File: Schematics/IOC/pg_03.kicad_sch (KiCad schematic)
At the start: 78 parts, among them U401 F245, U402 F245, U403 F245, U404 F245, U405 F244, U406 F244, U407 F244, U408 F244, U409 F04, U410 F04, U411 F04, U412 F163, U413 F04, U414 F02

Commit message: Align to grid
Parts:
- removed GF103, GF107, GF11, GF111, GF115, GF119, GF123, GF127, GF15, GF167, GF171, GF175, GF179, GF183, GF187, GF19, GF191, GF195, GF199, GF203, GF207, GF211, GF215, GF219, GF223, GF227, GF23, GF231, GF235, GF239, GF243, GF247, GF251, GF255, GF259, GF263, GF267, GF27, GF271, GF275, GF279, GF283, GF287, GF291, GF3, GF31, GF35, GF39, GF43, GF47, GF51, GF55, GF59, GF63, GF67, GF7, GF71, GF75, GF79, GF83, GF87, GF91, GF95, GF99: GF, symbol r1000:GF
- removed U401, U402, U403, U404: F245, symbol r1000:F245
- removed U405, U406, U407, U408: F244, symbol r1000:F244
- removed U409, U410, U411, U413: F04, symbol r1000:F04
- removed U412: F163, symbol r1000:F163
- removed U414: F02, symbol r1000:F02
- added U (x64): (no value), symbol r1000:GF
- added U (x4): (no value), symbol r1000:F04
- added U (x4): (no value), symbol r1000:F245
- added U (x4): (no value), symbol r1000:F244
- added U: (no value), symbol r1000:F02
- added U: (no value), symbol r1000:F163
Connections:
- net 68K.A0: now also U.2 (D1), U.2 (I0)
- net 68K.A1: now also U.4 (I1)
- net 68K.A10: now also U.6 (I2)
- net 68K.A11: now also U.8 (I3)
- net 68K.A12: now also U.11 (I4)
- net 68K.A13: now also U.13 (I5)
- net 68K.A14: now also U.15 (I6)
- net 68K.A15: now also U.17 (I7)
- net 68K.A16: now also U.2 (I0)
- net 68K.A17: now also U.4 (I1)
- net 68K.A18: now also U.6 (I2)
- net 68K.A19: now also U.8 (I3)
- net 68K.A2: now also U.6 (I2)
- net 68K.A20: now also U.11 (I4)
- net 68K.A21: now also U.13 (I5)
- net 68K.A22: now also U.15 (I6)
- net 68K.A23: now also U.17 (I7)
- net 68K.A24: now also U.2 (I0)
- net 68K.A25: now also U.4 (I1)
- net 68K.A26: now also U.6 (I2)
- net 68K.A27: now also U.8 (I3)
- net 68K.A28: now also U.11 (I4)
- net 68K.A29: now also U.13 (I5)
- net 68K.A3: now also U.8 (I3)
- net 68K.A30: now also U.15 (I6)
- net 68K.A31: now also U.17 (I7)
- net 68K.A4: now also U.11 (I4)
- net 68K.A5: now also U.13 (I5)
- net 68K.A6: now also U.15 (I6)
- net 68K.A7: now also U.17 (I7)
- net 68K.A8: now also U.2 (I0)
- net 68K.A9: now also U.4 (I1)
- net 68K.D0: now also U.2 (A0)
- net 68K.D1: now also U.3 (A1)
- net 68K.D10: now also U.4 (A2)
- net 68K.D11: now also U.5 (A3)
- net 68K.D12: now also U.6 (A4)
- net 68K.D13: now also U.7 (A5)
- net 68K.D14: now also U.8 (A6)
- net 68K.D15: now also U.9 (A7)
- net 68K.D16: now also U.2 (A0)
- net 68K.D17: now also U.3 (A1)
- net 68K.D18: now also U.4 (A2)
- net 68K.D19: now also U.5 (A3)
- net 68K.D2: now also U.4 (A2)
- net 68K.D20: now also U.6 (A4)
- net 68K.D21: now also U.7 (A5)
- net 68K.D22: now also U.8 (A6)
- net 68K.D23: now also U.9 (A7)
- net 68K.D24: now also U.2 (A0)
- net 68K.D25: now also U.3 (A1)
- net 68K.D26: now also U.4 (A2)
- net 68K.D27: now also U.5 (A3)
- net 68K.D28: now also U.6 (A4)
- net 68K.D29: now also U.7 (A5)
- net 68K.D3: now also U.5 (A3)
- net 68K.D30: now also U.8 (A6)
- net 68K.D31: now also U.9 (A7)
- net 68K.D4: now also U.6 (A4)
- net 68K.D5: now also U.7 (A5)
- net 68K.D6: now also U.8 (A6)
- net 68K.D7: now also U.9 (A7)
- net 68K.D8: now also U.2 (A0)
- net 68K.D9: now also U.3 (A1)
- net BOOTTIME: now also U.1 (D0), U.2 (Q), U.7 (ENP)
- net CLK.2X.B3: now also U.2 (CLK)
- net CYCLE_END: now also U.10 (ENT)
- net DBEN~: now also U.19 (OE), U.19 (OE), U.19 (OE), U.19 (OE)
- net IOP.A0~: now also U.1, U.3 (Q)
- net IOP.A1: now also U.1, U.16 (Y1)
- net IOP.A10: now also U.1, U.14 (Y2)
- net IOP.A11: now also U.1, U.12 (Y3)
- net IOP.A12: now also U.1, U.9 (Y4)
- net IOP.A13: now also U.1, U.7 (Y5)
- net IOP.A14: now also U.1, U.5 (Y6)
- net IOP.A15: now also U.1, U.3 (Y7)
- net IOP.A16: now also U.1, U.18 (Y0)
- net IOP.A17: now also U.1, U.16 (Y1)
- net IOP.A18: now also U.1, U.14 (Y2)
- net IOP.A19: now also U.1, U.12 (Y3)
- net IOP.A2: now also U.1, U.14 (Y2)
- net IOP.A20: now also U.1, U.9 (Y4)
- net IOP.A21: now also U.1, U.7 (Y5)
- net IOP.A22: now also U.1, U.5 (Y6)
- net IOP.A23: now also U.1, U.3 (Y7)
- net IOP.A24: now also U.1, U.18 (Y0)
- net IOP.A25: now also U.1, U.16 (Y1)
- net IOP.A26: now also U.1, U.14 (Y2)
- net IOP.A27: now also U.1, U.12 (Y3)
- net IOP.A28: now also U.1, U.9 (Y4)
- net IOP.A29: now also U.1, U.7 (Y5)
- net IOP.A3: now also U.1, U.12 (Y3)
- net IOP.A30: now also U.1, U.5 (Y6)
- net IOP.A31: now also U.1, U.3 (Y7)
- net IOP.A4: now also U.1, U.9 (Y4)
- net IOP.A5: now also U.1, U.7 (Y5)
- net IOP.A6: now also U.1, U.5 (Y6)
- net IOP.A7: now also U.1, U.3 (Y7)
- net IOP.A8: now also U.1, U.18 (Y0)
- net IOP.A9: now also U.1, U.16 (Y1)
- net IOP.D0: now also U.1, U.18 (B0)
- net IOP.D1: now also U.1, U.17 (B1)
- net IOP.D10: now also U.1, U.16 (B2)
- net IOP.D11: now also U.1, U.15 (B3)
- net IOP.D12: now also U.1, U.14 (B4)
- net IOP.D13: now also U.1, U.13 (B5)
- net IOP.D14: now also U.1, U.12 (B6)
- net IOP.D15: now also U.1, U.11 (B7)
- net IOP.D16: now also U.1, U.18 (B0)
- net IOP.D17: now also U.1, U.17 (B1)
- net IOP.D18: now also U.1, U.16 (B2)
- net IOP.D19: now also U.1, U.15 (B3)
- net IOP.D2: now also U.1, U.16 (B2)
- net IOP.D20: now also U.1, U.14 (B4)
- net IOP.D21: now also U.1, U.13 (B5)
- net IOP.D22: now also U.1, U.12 (B6)
- net IOP.D23: now also U.1, U.11 (B7)
- net IOP.D24: now also U.1, U.18 (B0)
- net IOP.D25: now also U.1, U.17 (B1)
- net IOP.D26: now also U.1, U.16 (B2)
- net IOP.D27: now also U.1, U.15 (B3)
- net IOP.D28: now also U.1, U.14 (B4)
- net IOP.D29: now also U.1, U.13 (B5)
- net IOP.D3: now also U.1, U.15 (B3)
- net IOP.D30: now also U.1, U.12 (B6)
- net IOP.D31: now also U.1, U.11 (B7)
- net IOP.D4: now also U.1, U.14 (B4)
- net IOP.D5: now also U.1, U.13 (B5)
- net IOP.D6: now also U.1, U.12 (B6)
- net IOP.D7: now also U.1, U.11 (B7)
- net IOP.D8: now also U.1, U.18 (B0)
- net IOP.D9: now also U.1, U.17 (B1)
- net IOP.WR.B0: now also U.1 (D0), U.1 (DIR), U.1 (DIR), U.1 (DIR), U.1 (DIR), U.2 (Q)
- net IOP.WR.B1: now also U.2 (Q)
- net IOP.WR~: now also U.2 (Q)
- net IOP_RESET~: now also U.1 (CLR)
- net PD: now also U.1 (OE0), U.1 (OE0), U.1 (OE0), U.1 (OE0), U.19 (OE1), U.19 (OE1), U.19 (OE1), U.19 (OE1)
- net PU: now also U.9 (LD)
- net WR~: now also U.1 (D0), U.1 (D0)
- new net: U.1 (D0), U.11 (Q0)

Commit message: TYP/VAL busses
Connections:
- net 68K.D0: now also U.3 (A0); no longer U.2 (A0)
- net 68K.D1: now also U.5 (A1); no longer U.3 (A1)
- net 68K.D10: now also U.7 (A2); no longer U.4 (A2)
- net 68K.D11: now also U.9 (A3); no longer U.5 (A3)
- net 68K.D12: now also U.11 (A4); no longer U.6 (A4)
- net 68K.D13: now also U.13 (A5); no longer U.7 (A5)
- net 68K.D14: now also U.15 (A6); no longer U.8 (A6)
- net 68K.D15: now also U.17 (A7); no longer U.9 (A7)
- net 68K.D16: now also U.3 (A0); no longer U.2 (A0)
- net 68K.D17: now also U.5 (A1); no longer U.3 (A1)
- net 68K.D18: now also U.7 (A2); no longer U.4 (A2)
- net 68K.D19: now also U.9 (A3); no longer U.5 (A3)
- net 68K.D2: now also U.7 (A2); no longer U.4 (A2)
- net 68K.D20: now also U.11 (A4); no longer U.6 (A4)
- net 68K.D21: now also U.13 (A5); no longer U.7 (A5)
- net 68K.D22: now also U.15 (A6); no longer U.8 (A6)
- net 68K.D23: now also U.17 (A7); no longer U.9 (A7)
- net 68K.D24: now also U.3 (A0); no longer U.2 (A0)
- net 68K.D25: now also U.5 (A1); no longer U.3 (A1)
- net 68K.D26: now also U.7 (A2); no longer U.4 (A2)
- net 68K.D27: now also U.9 (A3); no longer U.5 (A3)
- net 68K.D28: now also U.11 (A4); no longer U.6 (A4)
- net 68K.D29: now also U.13 (A5); no longer U.7 (A5)
- net 68K.D3: now also U.9 (A3); no longer U.5 (A3)
- net 68K.D30: now also U.15 (A6); no longer U.8 (A6)
- net 68K.D31: now also U.17 (A7); no longer U.9 (A7)
- net 68K.D4: now also U.11 (A4); no longer U.6 (A4)
- net 68K.D5: now also U.13 (A5); no longer U.7 (A5)
- net 68K.D6: now also U.15 (A6); no longer U.8 (A6)
- net 68K.D7: now also U.17 (A7); no longer U.9 (A7)
- net 68K.D8: now also U.3 (A0); no longer U.2 (A0)
- net 68K.D9: now also U.5 (A1); no longer U.3 (A1)
- net BOOTTIME: now also U.13 (ENP); no longer U.7 (ENP)
- net CLK.2X.B3: now also U.1 (CLK); no longer U.2 (CLK)
- net CYCLE_END: now also U.14 (ENT); no longer U.10 (ENT)
- net DBEN~: now also U.2 (OE), U.2 (OE), U.2 (OE), U.2 (OE); no longer U.19 (OE), U.19 (OE), U.19 (OE), U.19 (OE)
- net IOP.D0: now also U.4 (B0); no longer U.18 (B0)
- net IOP.D1: now also U.6 (B1); no longer U.17 (B1)
- net IOP.D10: now also U.8 (B2); no longer U.16 (B2)
- net IOP.D11: now also U.10 (B3); no longer U.15 (B3)
- net IOP.D12: now also U.12 (B4); no longer U.14 (B4)
- net IOP.D13: now also U.14 (B5); no longer U.13 (B5)
- net IOP.D14: now also U.16 (B6); no longer U.12 (B6)
- net IOP.D15: now also U.18 (B7); no longer U.11 (B7)
- net IOP.D16: now also U.4 (B0); no longer U.18 (B0)
- net IOP.D17: now also U.6 (B1); no longer U.17 (B1)
- net IOP.D18: now also U.8 (B2); no longer U.16 (B2)
- net IOP.D19: now also U.10 (B3); no longer U.15 (B3)
- net IOP.D2: now also U.8 (B2); no longer U.16 (B2)
- net IOP.D20: now also U.12 (B4); no longer U.14 (B4)
- net IOP.D21: now also U.14 (B5); no longer U.13 (B5)
- net IOP.D22: now also U.16 (B6); no longer U.12 (B6)
- net IOP.D23: now also U.18 (B7); no longer U.11 (B7)
- net IOP.D24: now also U.4 (B0); no longer U.18 (B0)
- net IOP.D25: now also U.6 (B1); no longer U.17 (B1)
- net IOP.D26: now also U.8 (B2); no longer U.16 (B2)
- net IOP.D27: now also U.10 (B3); no longer U.15 (B3)
- net IOP.D28: now also U.12 (B4); no longer U.14 (B4)
- net IOP.D29: now also U.14 (B5); no longer U.13 (B5)
- net IOP.D3: now also U.10 (B3); no longer U.15 (B3)
- net IOP.D30: now also U.16 (B6); no longer U.12 (B6)
- net IOP.D31: now also U.18 (B7); no longer U.11 (B7)
- net IOP.D4: now also U.12 (B4); no longer U.14 (B4)
- net IOP.D5: now also U.14 (B5); no longer U.13 (B5)
- net IOP.D6: now also U.16 (B6); no longer U.12 (B6)
- net IOP.D7: now also U.18 (B7); no longer U.11 (B7)
- net IOP.D8: now also U.4 (B0); no longer U.18 (B0)
- net IOP.D9: now also U.6 (B1); no longer U.17 (B1)
- net IOP_RESET~: now also U.3 (CLR); no longer U.1 (CLR)
- net PU: now also U.2 (LD); no longer U.9 (LD)
- net at U.11 (D3): no longer U.1 (D0)
- net at U.6 (Q0): now also U.1 (D0)

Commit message: IOC: dedup, clocks, dfsm
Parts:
- removed U: (no value), symbol r1000:F04
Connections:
- net CLK.2X.B3 renamed CLK.2X
- net IOP.WR.B0 renamed IOP.WR
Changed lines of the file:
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@@
   (junction (at 203.2 142.24) (diameter 0) (color 0 0 0 0)
   )
-  (junction (at 48.26 17.78) (diameter 0) (color 0 0 0 0)
-  )
   (junction (at 76.2 139.7) (diameter 0) (color 0 0 0 0)
   )
@@
     (stroke (width 0) (type default))
   )
-  (wire (pts (xy 48.26 35.56) (xy 48.26 17.78))
-    (stroke (width 0) (type default))
-  )
   (wire (pts (xy 487.68 68.58) (xy 492.76 68.58))
     (stroke (width 0) (type default))
@@
     (stroke (width 0) (type default))
   )
-  (wire (pts (xy 58.42 35.56) (xy 48.26 35.56))
-    (stroke (width 0) (type default))
-  )
   (wire (pts (xy 93.98 287.02) (xy 76.2 287.02))
     (stroke (width 0) (type default))
@@
     (stroke (width 0) (type default))
   )
-  (wire (pts (xy 40.64 17.78) (xy 48.26 17.78))
-    (stroke (width 0) (type default))
-  )
   (bus (pts (xy 246.38 182.88) (xy 246.38 187.96))
     (stroke (width 0) (type default))
@@
     (stroke (width 0) (type default))
   )
-  (wire (pts (xy 78.74 35.56) (xy 104.14 35.56))
-    (stroke (width 0) (type default))
-  )
   (bus (pts (xy 246.38 114.3) (xy 246.38 119.38))
     (stroke (width 0) (type default))
@@
     (stroke (width 0) (type default))
   )
-  (wire (pts (xy 48.26 17.78) (xy 58.42 17.78))
+  (wire (pts (xy 40.64 17.78) (xy 58.42 17.78))
     (stroke (width 0) (type default))
   )
@@
     (effects (font (size 2.54 2.54)) (justify left bottom))
   )
-  (label "IOP.WR.B0" (at 162.56 40.64 0) (fields_autoplaced)
+  (label "IOP.WR" (at 162.56 40.64 0) (fields_autoplaced)
     (effects (font (size 2.54 2.54)) (justify left bottom))
   )
@@
     )
   )
-  (global_label "IOP.WR.B0" (shape input) (at 40.64 60.96 180) (fields_autoplaced)
+  (global_label "IOP.WR" (shape input) (at 40.64 60.96 180) (fields_autoplaced)
     (effects (font (size 2.54 2.54)) (justify right))
     (property "Intersheet References" "${INTERSHEET_REFS}" (id 0) (at 16.2016 60.8013 0)
@@
     )
   )
-  (global_label "IOP.WR.B0" (shape output) (at 104.14 17.78 0) (fields_autoplaced)
+  (global_label "IOP.WR" (shape output) (at 104.14 17.78 0) (fields_autoplaced)
     (effects (font (size 2.54 2.54)) (justify left))
     (property "Intersheet References" "${INTERSHEET_REFS}" (id 0) (at 128.5784 17.6213 0)
@@
     )
   )
-  (global_label "CLK.2X.B3" (shape input) (at 297.18 40.64 180) (fields_autoplaced)
+  (global_label "CLK.2X" (shape input) (at 297.18 40.64 180) (fields_autoplaced)
     (effects (font (size 2.54 2.54)) (justify right))
     (property "Intersheet References" "${INTERSHEET_REFS}" (id 0) (at 272.6206 40.4813 0)
@@
     )
   )
-  (global_label "IOP.WR.B1" (shape output) (at 104.14 35.56 0) (fields_autoplaced)
-    (effects (font (size 2.54 2.54)) (justify left))
-    (property "Intersheet References" "${INTERSHEET_REFS}" (id 0) (at 128.5784 35.4013 0)
-      (effects (font (size 1.905 1.905)) (justify left))
-    )
-  )
   (symbol (lib_id "r1000:GF") (at 337.82 228.6 0) (unit 1)
     (in_bom yes) (on_board yes)
@@
     (pin "1")
   )
-  (symbol (lib_id "r1000:F04") (at 68.58 35.56 0) (unit 1)
-    (in_bom yes) (on_board yes)
-    (default_instance (reference "U") (unit 1) (value "") (footprint ""))
-    (property "Reference" "U" (id 0) (at 68.58 35.56 0)
-      (effects (font (size 1.27 1.27)))
-    )
-    (property "Value" "" (id 1) (at 69.85 40.64 0)
-      (effects (font (size 2.54 2.54)) (justify left))
-    )
-    (property "Footprint" "" (id 2) (at 68.58 35.56 0)
-      (effects (font (size 1.27 1.27)) hide)
-    )
-    (property "Datasheet" "" (id 3) (at 68.58 35.56 0)
-      (effects (font (size 1.27 1.27)) hide)
-    )
-    (property "Location" "I5" (id 4) (at 55.88 40.64 0)
-      (effects (font (size 2.54 2.54)) (justify left))
-    )
-    (property "Name" "IPINV0F" (id 5) (at 68.58 30.48 0)
-      (effects (font (size 2.54 2.54)) (justify bottom))
-    )
-    (pin "1")
-    (pin "2")
-  )
   (symbol (lib_id "r1000:GF") (at 274.32 248.92 0) (unit 1)

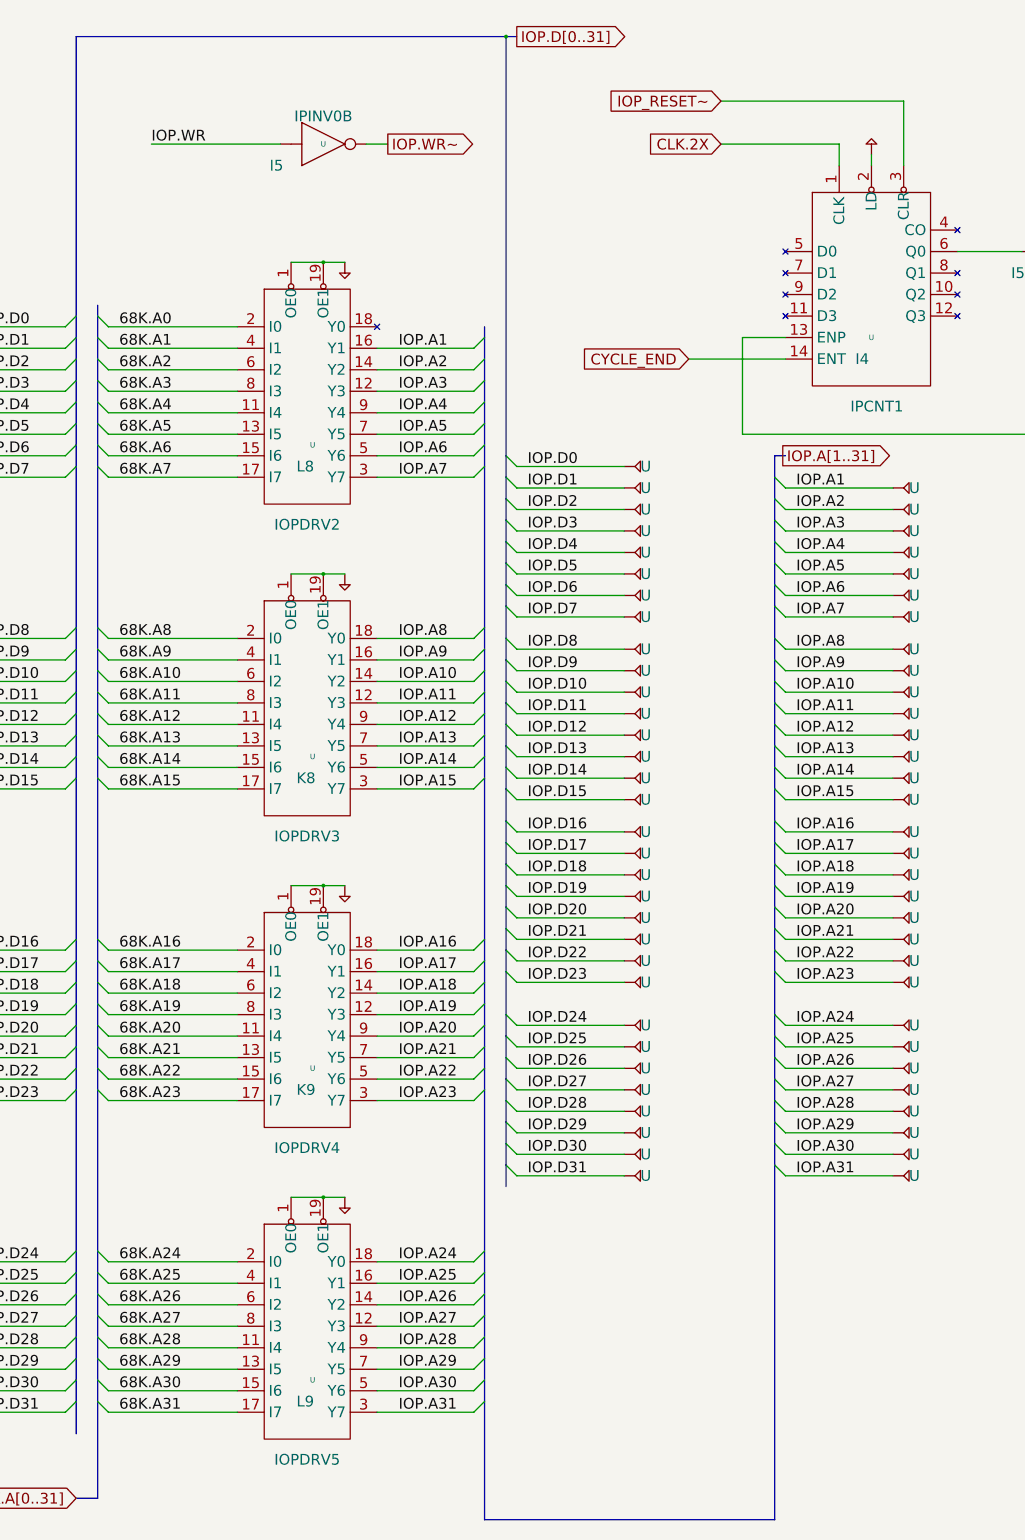
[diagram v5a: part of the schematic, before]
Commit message: IOC: Redo, dedup, clocks
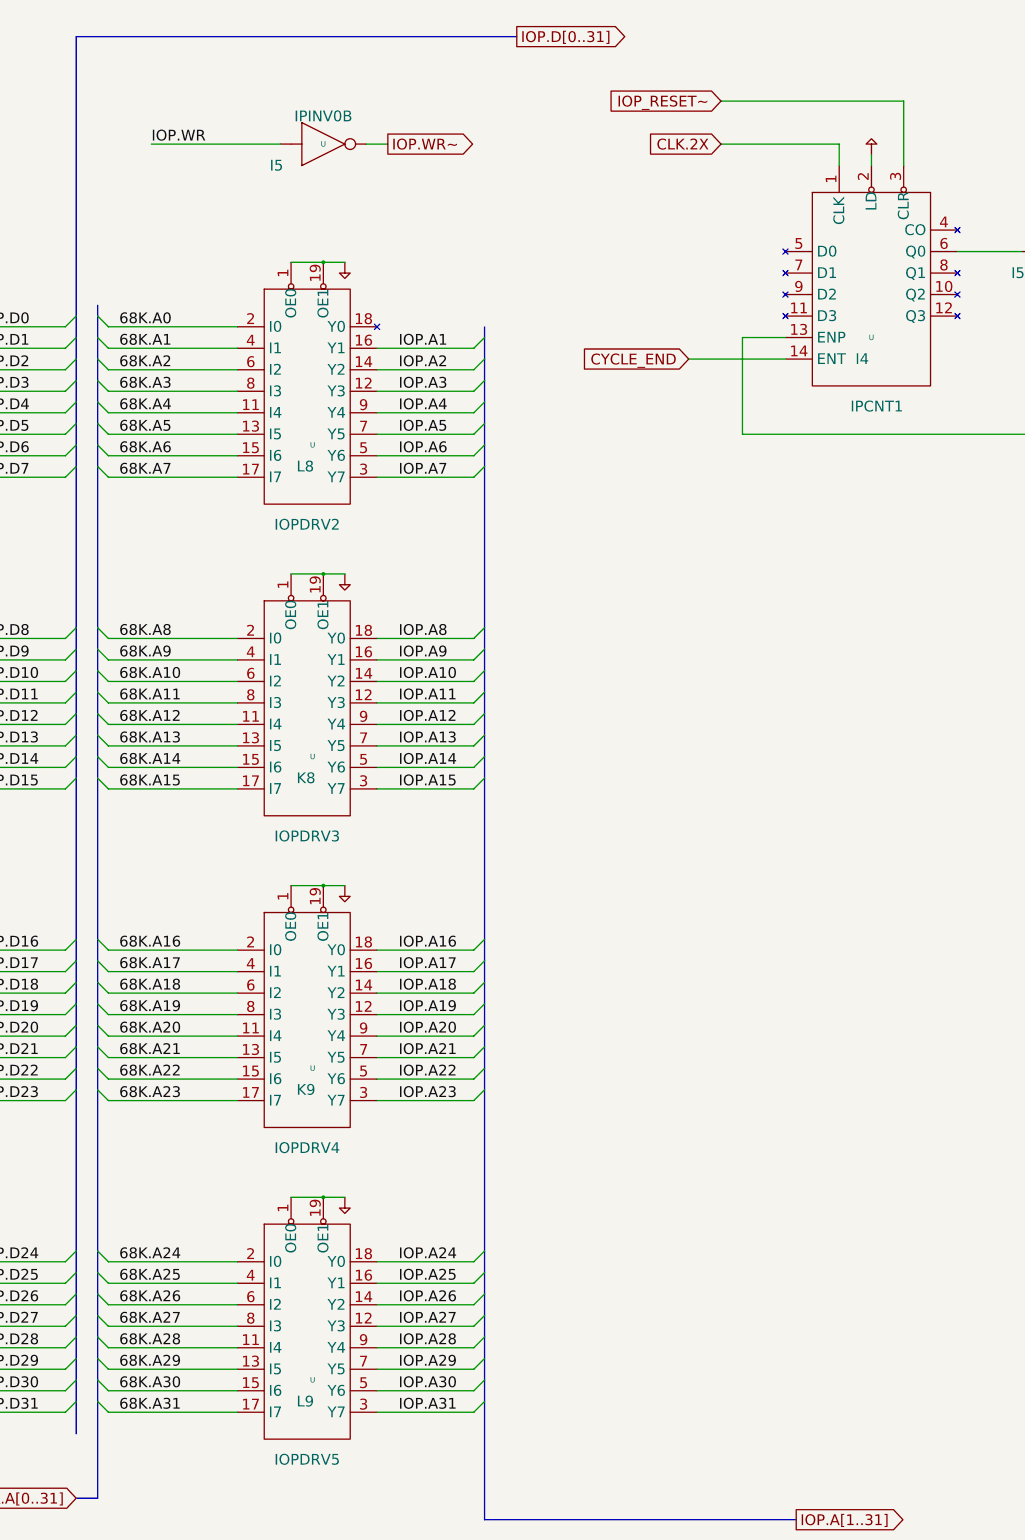
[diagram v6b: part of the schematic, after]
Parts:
- removed U (x63): (no value), symbol r1000:GF

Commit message: IOC/RESHA cleanup, tested to 6 seconds (@c11)
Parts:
- removed U (x4): (no value), symbol r1000:F245
- removed U (x4): (no value), symbol r1000:F244
- removed U: (no value), symbol r1000:F02
- removed U: (no value), symbol r1000:F163
- removed U: (no value), symbol r1000:GF
- removed U: (no value), symbol r1000:F04
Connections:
- no-connect marks 9 -> 0

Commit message: Tested to 21.6 seconds (rm073)
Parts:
- removed U: (no value), symbol r1000:F04
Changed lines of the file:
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@@
     (comment 4 "RELEASED")
-  )
-  (wire (pts (xy 213.36 40.64) (xy 218.44 40.64))
-    (stroke (width 0) (type default))
-  )
-  (wire (pts (xy 162.56 40.64) (xy 193.04 40.64))
-    (stroke (width 0) (type default))
   )
   (wire (pts (xy 78.74 17.78) (xy 104.14 17.78))
@@
     (stroke (width 0) (type default))
   )
-  (label "IOP.WR" (at 162.56 40.64 0) (fields_autoplaced)
-    (effects (font (size 2.54 2.54)) (justify left bottom))
-  )
   (global_label "WR~" (shape input) (at 40.64 17.78 180) (fields_autoplaced)
     (effects (font (size 2.54 2.54)) (justify right))
     (property "Intersheet References" "${INTERSHEET_REFS}" (id 0) (at 28.1759 17.6213 0)
       (effects (font (size 1.905 1.905)) (justify right))
-    )
-  )
-  (global_label "IOP.WR~" (shape output) (at 218.44 40.64 0) (fields_autoplaced)
-    (effects (font (size 2.54 2.54)) (justify left))
-    (property "Intersheet References" "${INTERSHEET_REFS}" (id 0) (at 238.5241 40.4813 0)
-      (effects (font (size 1.905 1.905)) (justify left))
     )
   )
@@
     )
   )
-  (symbol (lib_id "r1000:F04") (at 203.2 40.64 0) (unit 1)
-    (in_bom yes) (on_board yes)
-    (default_instance (reference "U") (unit 1) (value "") (footprint ""))
-    (property "Reference" "U" (id 0) (at 203.2 40.64 0)
-      (effects (font (size 1.27 1.27)))
-    )
-    (property "Value" "" (id 1) (at 204.47 45.72 0)
-      (effects (font (size 2.54 2.54)) (justify left))
-    )
-    (property "Footprint" "" (id 2) (at 203.2 40.64 0)
-      (effects (font (size 1.27 1.27)) hide)
-    )
-    (property "Datasheet" "" (id 3) (at 203.2 40.64 0)
-      (effects (font (size 1.27 1.27)) hide)
-    )
-    (property "Location" "I5" (id 4) (at 190.5 45.72 0)
-      (effects (font (size 2.54 2.54)) (justify left))
-    )
-    (property "Name" "IPINV0B" (id 5) (at 203.2 35.56 0)
-      (effects (font (size 2.54 2.54)) (justify bottom))
-    )
-    (pin "1")
-    (pin "2")
-  )
   (symbol (lib_id "r1000:F04") (at 68.58 17.78 0) (unit 1)
